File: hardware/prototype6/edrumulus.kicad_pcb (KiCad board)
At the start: 2 copper layers, 196.7 x 84.6 mm, 106 parts, among them J1 Hi-Hat, J10 MIDI-IN, J11 MIDI-OUT, J2 Snare, J3 Crash, J4 Ride, J5 Tom1, J6 Tom2, J7 Tom3, J8 Kick, J9 Hi-Hat-Ctrl, U1 ESP32-DEVKIT-V1, U2 6N138, U3 L78L33_TO92

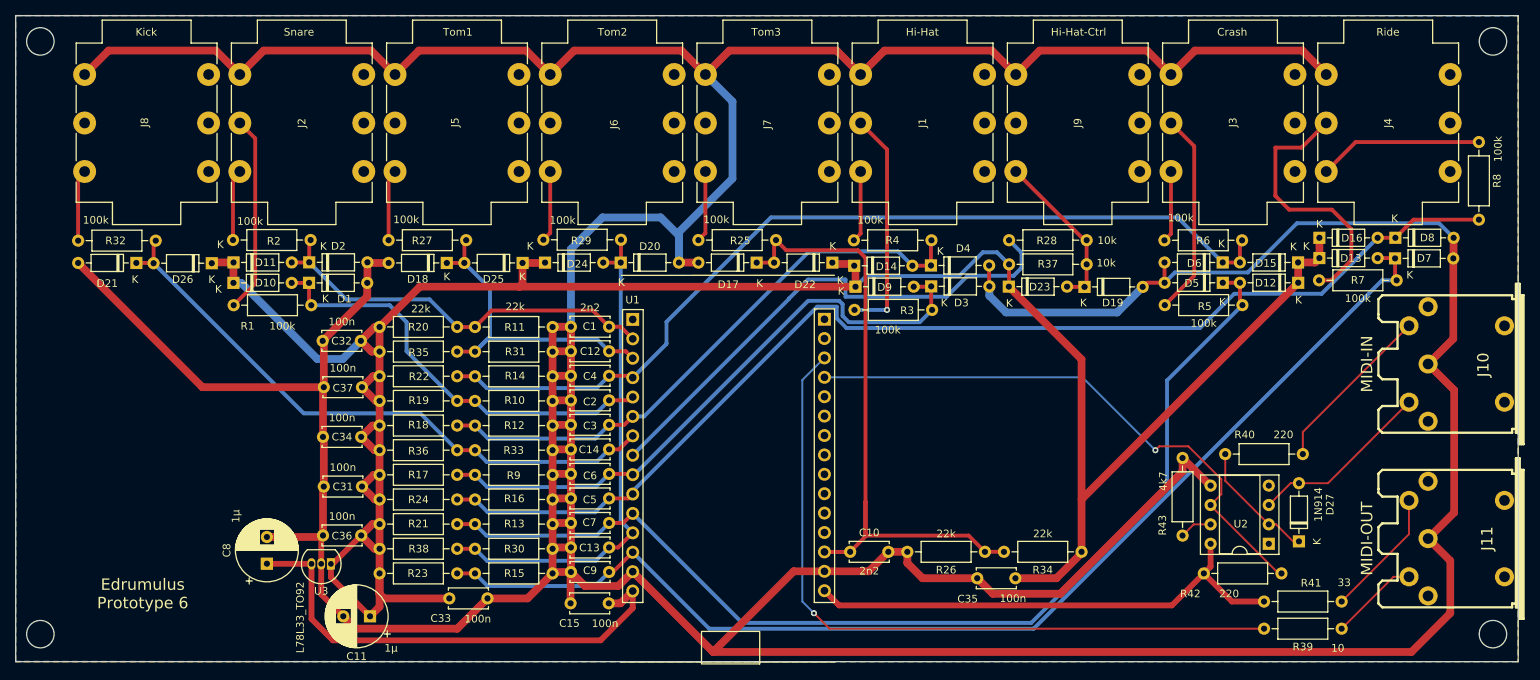
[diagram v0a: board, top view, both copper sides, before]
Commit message: change prototype identification for prototype 6
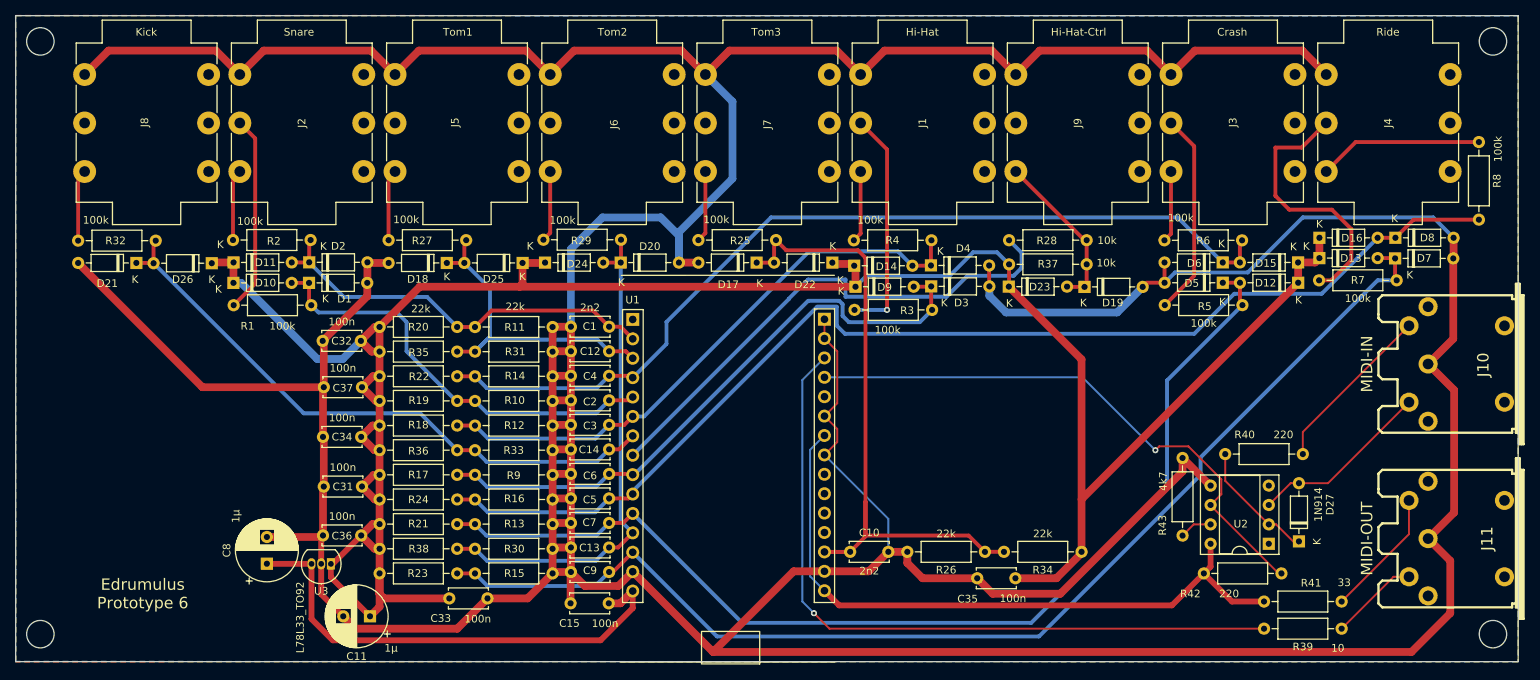
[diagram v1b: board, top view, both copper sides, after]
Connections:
- C1 pad 2: GND -> GPIO5
- C10 pad 2: GND -> GPIO5
- C11 pad 2: GND -> GPIO5
- C12 pad 2: GND -> GPIO5
- C13 pad 2: GND -> GPIO5
- C14 pad 2: GND -> GPIO5
- C15 pad 2: GND -> GPIO5
- C2 pad 2: GND -> GPIO5
- C3 pad 2: GND -> GPIO5
- C31 pad 2: GND -> GPIO5
- C32 pad 2: GND -> GPIO5
- C33 pad 2: GND -> GPIO5
- C34 pad 2: GND -> GPIO5
- C35 pad 2: GND -> GPIO5
- C36 pad 2: GND -> GPIO5
- C37 pad 2: GND -> GPIO5
- C4 pad 2: GND -> GPIO5
- C5 pad 2: GND -> GPIO5
- C6 pad 2: GND -> GPIO5
- C7 pad 2: GND -> GPIO5
- C8 pad 2: GND -> GPIO5
- C9 pad 2: GND -> GPIO5
- D1 pad 2: GND -> GPIO5
- D17 pad 2: GND -> GPIO5
- D18 pad 2: GND -> GPIO5
- D19 pad 2: GND -> GPIO5
- D2 pad 2: GND -> GPIO5
- D20 pad 2: GND -> GPIO5
- D21 pad 2: GND -> GPIO5
- D3 pad 2: GND -> GPIO5
- D4 pad 2: GND -> GPIO5
- D5 pad 2: GND -> GPIO5
- D6 pad 2: GND -> GPIO5
- D7 pad 2: GND -> GPIO5
- D8 pad 2: GND -> GPIO5
- J1 pad S: GND -> GPIO5
- J10 pad 2: GND -> GPIO5
- J11 pad 2: GND -> GPIO5
- J2 pad S: GND -> GPIO5
- J3 pad S: GND -> GPIO5
- J4 pad S: GND -> GPIO5
- J5 pad S: GND -> GPIO5
- J6 pad S: GND -> GPIO5
- J7 pad S: GND -> GPIO5
- J8 pad S: GND -> GPIO5
- J9 pad S: GND -> GPIO5
- R10 pad 2: GND -> GPIO5
- R11 pad 2: GND -> GPIO5
- R12 pad 2: GND -> GPIO5
- R13 pad 2: GND -> GPIO5
- R14 pad 2: GND -> GPIO5
- R15 pad 2: GND -> GPIO5
- R16 pad 2: GND -> GPIO5
- R26 pad 2: GND -> GPIO5
- R30 pad 2: GND -> GPIO5
- R31 pad 2: GND -> GPIO5
- R33 pad 2: GND -> GPIO5
- R41 pad 1: ESP-3V3 -> GPIO18
- R42 pad 2: ESP-3V3 -> GPIO18
- R43 pad 1: GND -> GPIO5
- R9 pad 2: GND -> GPIO5
- U1 pad 14: GND -> GPIO5
- U1 pad 16: ESP-3V3 -> GPIO18
- U1 pad 17: GND -> GPIO5
- U1 pad 23: unconnected-(U1-Pad23) -> GPIO5
- U1 pad 24: unconnected-(U1-Pad24) -> GPIO18
- U1 pad 25: unconnected-(U1-Pad25) -> GPIO5
- U1 pad 29: unconnected-(U1-Pad29) -> GPIO5
- U1 pad 30: unconnected-(U1-Pad30) -> GPIO5
- U2 pad 5: GND -> GPIO5
- U2 pad 8: ESP-3V3 -> GPIO18
- U3 pad 2: GND -> GPIO5
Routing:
- net GPIO5: track 0.00 -> 843.6 mm
- net GND: track 806.3 -> 0.00 mm
- net GPIO18: track 0.00 -> 87.7 mm
- net ESP-3V3: track 65.9 -> 0.00 mm
- net GPIO13: track 153.8 -> 156.0 mm
- net GPIO27: track 153.8 -> 155.0 mm
- added copper zone on B.Cu, net GPIO5
- added copper zone on F.Cu, net GPIO5
- removed copper zone on B.Cu, net GND
- removed copper zone on F.Cu, net GND
